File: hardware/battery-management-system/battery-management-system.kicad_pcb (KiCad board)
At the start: 4 copper layers, 100 x 111 mm, 212 parts, among them J1 CELL4_PLUS, J10 18V, J11 3V3, J12 AMPHENOL_micro_usb_10118194-0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, J13 I2C, J14 UART_INTERCONNECT, J15 LEDS, J16 CHARGE/DISCHARGE, J17 UART_USB, J18 rspro_header_5pin_3_5mm, J19 TEMP_CELL1, J2 CELL4_MINUS, J20 TEMP_CELL2, J21 TEMP_CELL3, J22 TEMP_CELL4, J23 Conn_01x05, J24 Charge, J25 Discharge, J3 CELL3_MINUS, J4 CELL2_MINUS, J5 CELL1_MINUS, J6 VBAT+, J7 VBAT+_CHARGE, J8 VBAT-, J9 5V, Q1 DMN3404L, Q10 DMN3404L, Q11 BS250FTA, Q12 BS250FTA, Q13 BS250FTA, Q14 BS250FTA, Q15 BS250FTA, Q16 DMN3404L, Q17 DMN3404L, Q18 DMN3404L, Q19 DMN3404L, Q2 TJ40S04M3L, Q20 DMN3404L, Q21 DMN3404L, Q22 DMN3404L, Q23 DMN3404L, Q24 DMN3404L, Q25 DMN3404L, Q26 DMN3404L, Q27 DMN3404L, Q28 DMN3404L, Q29 DMN3404L, Q3 TJ40S04M3L, Q30 DMN3404L, Q31 DMN3404L, Q32 DMN3404L, Q33 DMN3404L, Q34 DMN3404L, Q35 DMN3404L, Q36 DMN3404L, Q37 DMN3404L, Q38 DMN3404L, Q39 DMN3404L, Q4 DMN3404L, Q40 TJ40S04M3L, Q5 DMN3404L, Q6 DMN3404L, Q7 DMN3404L, Q8 DMN3404L, Q9 DMN3404L, U1 ICL7660, U10 STM32L071CZTx, U11 LM2904M8-13, U12 LM2904M8-13, U13 MC74VHC139, U2 L6982C33DR, U3 L6982C33DR, U4 ICL7660, U5 FT230XS, U6 ARM-JTAG-SWD, U7 AT24C512C, U8 NCT75DR2G, U9 STC3100

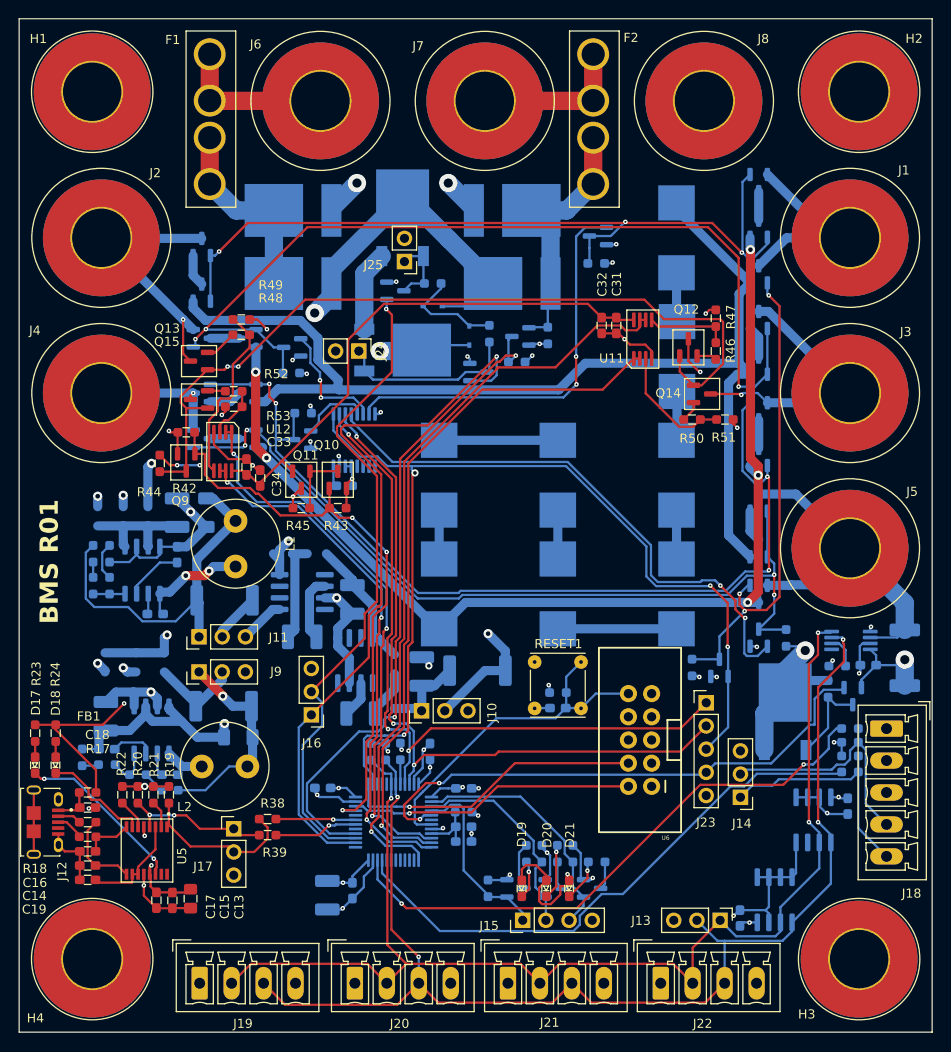
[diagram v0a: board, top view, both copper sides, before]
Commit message: update PCB from schematic
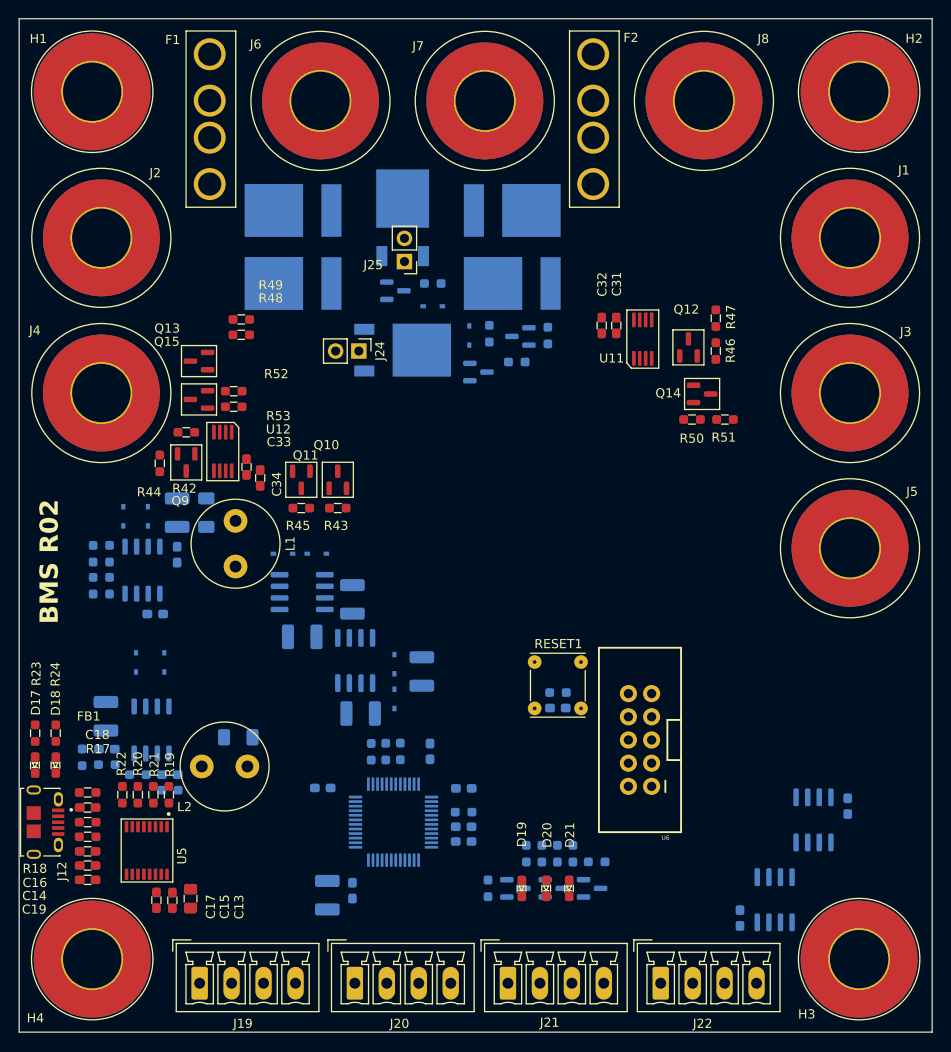
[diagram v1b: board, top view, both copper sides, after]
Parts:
- removed C30: 1uF, benediktibk:C_0603_1608Metric_Pad1.08x0.95mm_HandSolder
- removed C35: 100nF, benediktibk:C_0603_1608Metric_Pad1.08x0.95mm_HandSolder
- removed D15, D9: BAT54WS, benediktibk:D_SOD-323
- removed J10: 18V, benediktibk:PinHeader_1x03_P2.54mm_Vertical
- removed J11: 3V3, benediktibk:PinHeader_1x03_P2.54mm_Vertical
- removed J13: I2C, benediktibk:PinHeader_1x03_P2.54mm_Vertical
- removed J14: UART_INTERCONNECT, benediktibk:PinHeader_1x03_P2.54mm_Vertical
- removed J15: LEDS, benediktibk:PinHeader_1x04_P2.54mm_Vertical
- removed J16: CHARGE/DISCHARGE, benediktibk:PinHeader_1x03_P2.54mm_Vertical
- removed J17: UART_USB, benediktibk:PinHeader_1x03_P2.54mm_Vertical
- removed J18: rspro_header_5pin_3_5mm, benediktibk:rspro_header_5pin_3_5mm
- removed J23: Conn_01x05, benediktibk:PinHeader_1x05_P2.54mm_Vertical
- removed J9: 5V, benediktibk:PinHeader_1x03_P2.54mm_Vertical
- removed L10, L3, L4, L5, L6, L7, L8, L9: L_220µH_1A, benediktibk:L_Wuerth_HCI-1050
- removed Q16, Q17, Q18, Q19, Q20, Q21, Q22, Q23, Q24, Q25, Q26, Q27, Q28, Q29, Q30, Q31, Q32, Q33, Q34, Q35, Q36, Q37, Q38, Q39: DMN3404L, benediktibk:SOT-23
- removed Q40: TJ40S04M3L, benediktibk:TO-252-2
- removed R1, R14, R15, R16: 2mOhm, benediktibk:R_2512_6332Metric_Pad1.40x3.35mm_HandSolder
- removed R33: 200kOhm, benediktibk:R_0603_1608Metric_Pad0.98x0.95mm_HandSolder
- removed R35, R36, R38, R39: 0Ohm, benediktibk:R_0603_1608Metric_Pad0.98x0.95mm_HandSolder
- removed R40, R41, R54, R55, R56, R57, R58: 10kOhm, benediktibk:R_0603_1608Metric_Pad0.98x0.95mm_HandSolder
- removed R59: 220kOhm, benediktibk:R_0603_1608Metric_Pad0.98x0.95mm_HandSolder
- removed U13: MC74VHC139, benediktibk:TSSOP-16_4.4x5mm_P0.65mm
- removed U9: STC3100, benediktibk:MSOP-8_3x3mm_P0.65mm
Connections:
- C10 pad 1: Net-(D13-K) -> /18V
- C11 pad 1: Net-(J11-Pin_1) -> /3V3
- C12 pad 1: Net-(J9-Pin_1) -> Net-(D14-A)
- D13 pad 1: Net-(D13-K) -> /18V
- J5 pad 1: /Battery Pack/CELL1_MINUS -> GND
- L1 pad 1: Net-(J11-Pin_1) -> /3V3
- L2 pad 1: Net-(J9-Pin_1) -> Net-(D14-A)
- R10 pad 1: Net-(J9-Pin_1) -> Net-(D14-A)
- R6 pad 1: Net-(J11-Pin_1) -> /3V3
- U10 pad 21: Net-(U10-PB10) -> unconnected-(U10-PB10-Pad21)
- U10 pad 22: Net-(U10-PB11) -> unconnected-(U10-PB11-Pad22)
- U10 pad 30: Net-(U10-PA9) -> /MCU/UART_USB_TX
- U10 pad 31: Net-(U10-PA10) -> /MCU/UART_USB_RX
- U10 pad 38: /CELL_BALANCING_STROBE -> unconnected-(U10-PA15-Pad38)
- U10 pad 45: /CELL_BALANCING_A0 -> unconnected-(U10-PB8-Pad45)
- U10 pad 46: /CELL_BALANCING_A1 -> unconnected-(U10-PB9-Pad46)
- U10 pad 5: /EN_CELL_BALANCING -> unconnected-(U10-PH0-Pad5)
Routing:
- net GND: track 206.8 -> 0.00 mm, vias 41 -> 0
- net /18V: track 176.6 -> 0.00 mm, vias 8 -> 0
- net /5V_EXT: track 158.5 -> 0.00 mm, vias 2 -> 0
- net /MCU/SDA: track 136.1 -> 0.00 mm, vias 4 -> 0
- net /MCU/SCL: track 133.2 -> 0.00 mm, vias 3 -> 0
- net /5V: track 123.3 -> 0.00 mm, vias 3 -> 0
- net Net-(Q25-S): track 122.8 -> 0.00 mm
- net Net-(Q24-S): track 120.2 -> 0.00 mm, vias 5 -> 0
- net /CELL_BALANCING_STROBE: track 111.9 -> 0.00 mm, vias 4 -> 0
- net /PACK_EXT: track 104.5 -> 0.00 mm, vias 3 -> 0
- net /Cell Balancing/CHARGE_CELL2: track 103.4 -> 0.00 mm, vias 4 -> 0
- net /Cell Balancing/CHARGE_CELL3: track 101.9 -> 0.00 mm, vias 3 -> 0
- net /Battery Pack/PACK: track 95.8 -> 0.00 mm, vias 2 -> 0
- net /Cell Balancing/CHARGE_CELL1: track 91.8 -> 0.00 mm, vias 4 -> 0
- net Net-(Q12-G): track 91.1 -> 0.00 mm, vias 2 -> 0
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- removed copper zone on In1.Cu, net /3V3
- removed copper zone on In2.Cu, net GND
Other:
- board text added: "BMS R02"
- board text removed: "BMS R01"

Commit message: fix design errors
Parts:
- added C34: 100nF, benediktibk:C_0603_1608Metric_Pad1.08x0.95mm_HandSolder, F.Cu at (233.7, 96.5)
- added C35: 100nF, benediktibk:C_0603_1608Metric_Pad1.08x0.95mm_HandSolder, F.Cu at (233.7, 99.0)
- added C36: 100nF, benediktibk:C_0603_1608Metric_Pad1.08x0.95mm_HandSolder, F.Cu at (233.7, 101.5)
- added C37: 100nF, benediktibk:C_0603_1608Metric_Pad1.08x0.95mm_HandSolder, F.Cu at (233.7, 104.0)
- added R1: 220kOhm, benediktibk:R_0603_1608Metric_Pad0.98x0.95mm_HandSolder, F.Cu at (240.0, 96.5)
- added R3: 220kOhm, benediktibk:R_0603_1608Metric_Pad0.98x0.95mm_HandSolder, F.Cu at (240.0, 99.0)
- U2, U3: value L6982C33DR -> L6982CDR
- moved C2 108.6 mm to (145.9, 75.2)
- moved C31 108.6 mm to (192.4, 54.7)
- moved C5 108.6 mm to (145.9, 79.8)
- moved D1 108.6 mm to (177.9, 55.8)
- moved D14 108.6 mm to (141.4, 91.6)
- moved D17 108.6 mm to (183.6, 116.3)
- moved D2 108.6 mm to (173.9, 52.6)
- moved FB2 108.6 mm to (177.2, 108.0)
- moved Q1 108.6 mm to (178.9, 59.8)
- moved Q12 108.6 mm to (201.9, 57.1)
- moved Q14 108.6 mm to (203.4, 62.2)
- moved Q7 108.6 mm to (187.1, 116.3)
- moved Q9 108.6 mm to (146.9, 69.7)
- moved R20 108.6 mm to (139.9, 106.1)
- moved R24 108.6 mm to (184.1, 112.5)
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- renumbered C31 to C30, C32 to C31, C33 to C32, C34 to C33, D11 to D10, D12 to D11, D13 to D12, D14 to D13, D16 to D14, D17 to D15, D18 to D16, D19 to D17, D20 to D18, D21 to D19, D10 to D9, J8 to J10, J12 to J11, J19 to J12, J20 to J13, J21 to J14, J22 to J15, J24 to J6, J25 to J7, J6 to J8, J7 to J9, R9 to R10, R10 to R11, R11 to R12, R12 to R13, R13 to R14, R17 to R15, R18 to R16, R19 to R17, R20 to R18, R21 to R19, R22 to R20, R23 to R21, R24 to R22, R25 to R23, R26 to R24, R27 to R25, R28 to R26, R29 to R27, R30 to R28, R31 to R29, R32 to R30, R34 to R31, R37 to R32, R42 to R33, R43 to R34, R44 to R35, R45 to R36, R46 to R37, R47 to R38, R48 to R39, R3 to R4, R49 to R40, R50 to R41, R51 to R42, R52 to R43, R53 to R44, R4 to R5, R5 to R6, R6 to R7, R7 to R8, R8 to R9, U11 to U10, U12 to U11, U10 to U9
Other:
- board size 100 x 111 mm -> 100 x 100 mm

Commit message: fix design errors
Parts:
- removed the D5 at (158.6, 42.1)
- removed the D6 at (182.6, 42.1)
- removed the J10 at (203.6, 30.1)
- removed the J2 at (137.6, 45.1)
- removed the J3 at (219.6, 62.1)
- removed the J8 at (161.6, 30.1)
- removed the J9 at (179.6, 30.1)
- J1: value CELL4_PLUS -> CELLS; footprint benediktibk:Connector_M6 -> benediktibk:rspro_header_5pin_5_08mm
- J4: value CELL2_MINUS -> VBAT_DISCHARGE; footprint benediktibk:Connector_M6 -> benediktibk:rspro_header_2pin_5_08mm
- J5: value CELL1_MINUS -> VBAT_CHARGE; footprint benediktibk:Connector_M6 -> benediktibk:rspro_header_2pin_5_08mm
- J7: renamed from U6; footprint benediktibk:ARM-JTAG-10-SWD-IDC -> benediktibk:SAMTEC_FTSH-105-01-F-DV-P-TR
- moved J1 170.5 mm to (50.0, 27.0)
- moved J5 133.2 mm to (97.0, 27.0)
- moved J8 109.2 mm to (39.8, 114.6)
- moved D13 104.9 mm to (26.1, 90.8)
- moved D14 104.9 mm to (28.4, 90.8)
- moved J6 104.9 mm to (26.0, 97.0)
- moved R21 104.9 mm to (26.1, 87.2)
- moved R22 104.9 mm to (28.4, 87.2)
- moved R20 102.8 mm to (37.8, 93.4)
- moved C13 102.8 mm to (45.3, 104.8)
- moved C14 102.8 mm to (34.0, 101.2)
- moved C15 102.8 mm to (43.3, 105.0)
- moved C16 102.8 mm to (34.0, 99.6)
- moved C17 102.8 mm to (41.5, 105.0)
- moved C18 102.8 mm to (34.0, 94.8)
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- renumbered D12 to D10, D13 to D11, D14 to D12, D15 to D13, D16 to D14, D17 to D15, D18 to D16, D19 to D17, D7 to D5, D8 to D6, D9 to D7, D10 to D8, D11 to D9, J14 to J10, J15 to J11, J6 to J2, J7 to J3, J11 to J6, J12 to J8, J13 to J9, U11 to U10, U7 to U6, U8 to U7, U9 to U8, U10 to U9
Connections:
- F1 pad 1: Net-(J8-Pin_1) -> Net-(J4-Pin_1)
- F2 pad 1: Net-(J9-Pin_1) -> Net-(J5-Pin_1)
- J4 pad 1: /Battery Pack/CELL2_MINUS -> Net-(J4-Pin_1)
- J5 pad 1: GND -> Net-(J5-Pin_1)

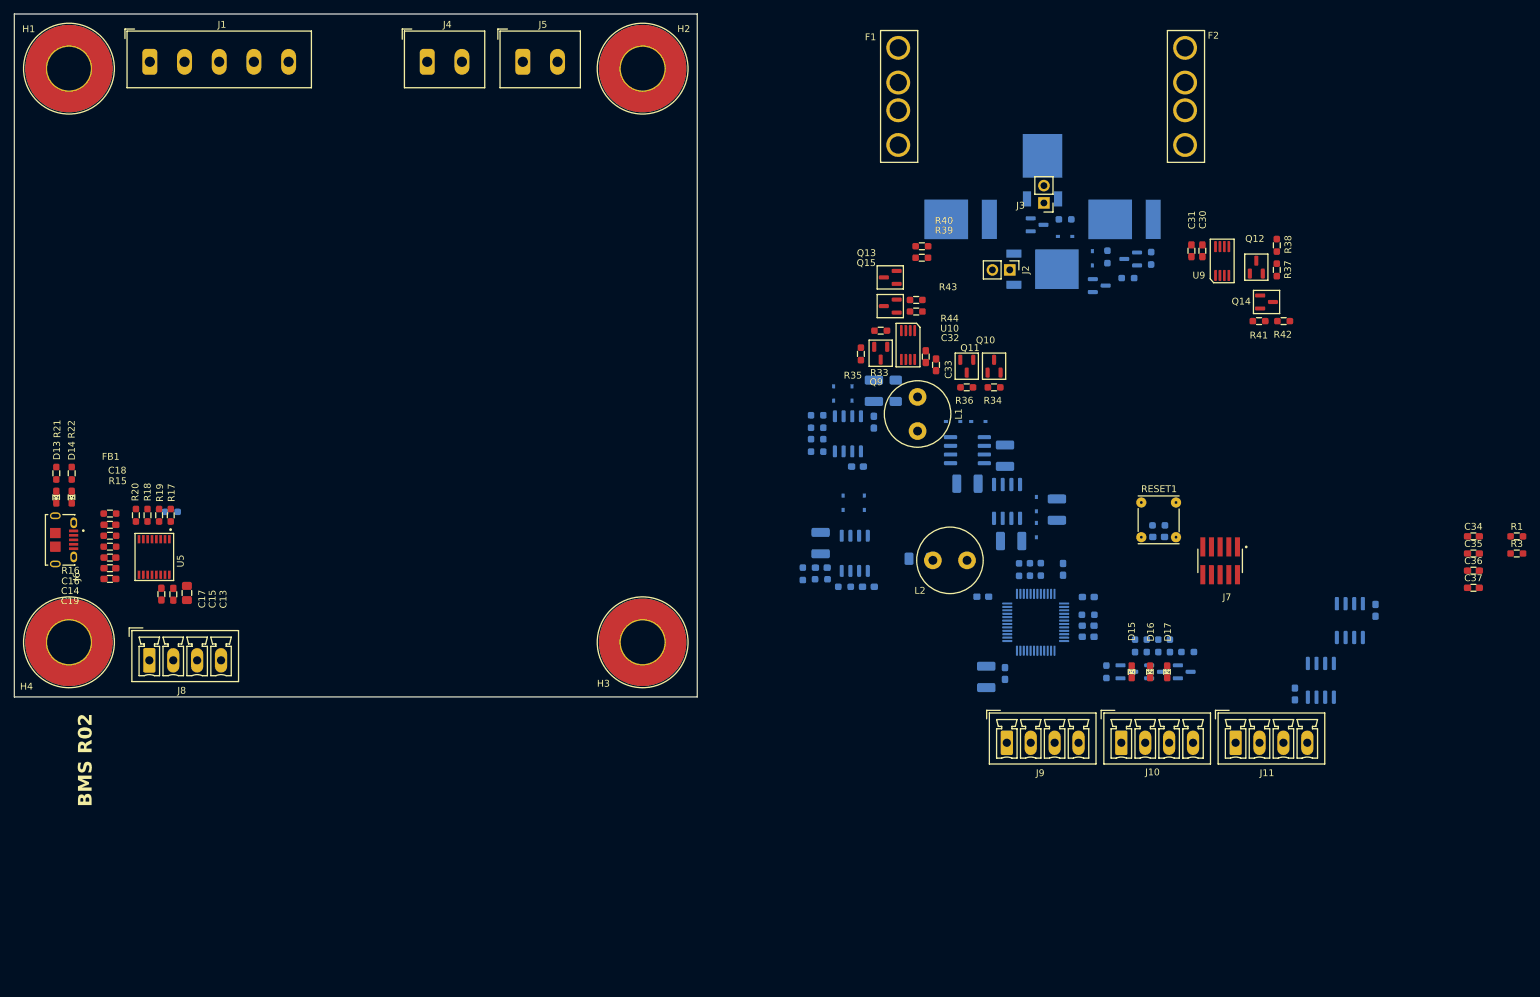
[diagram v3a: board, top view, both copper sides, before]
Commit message: add heatsink and fix ERC errors
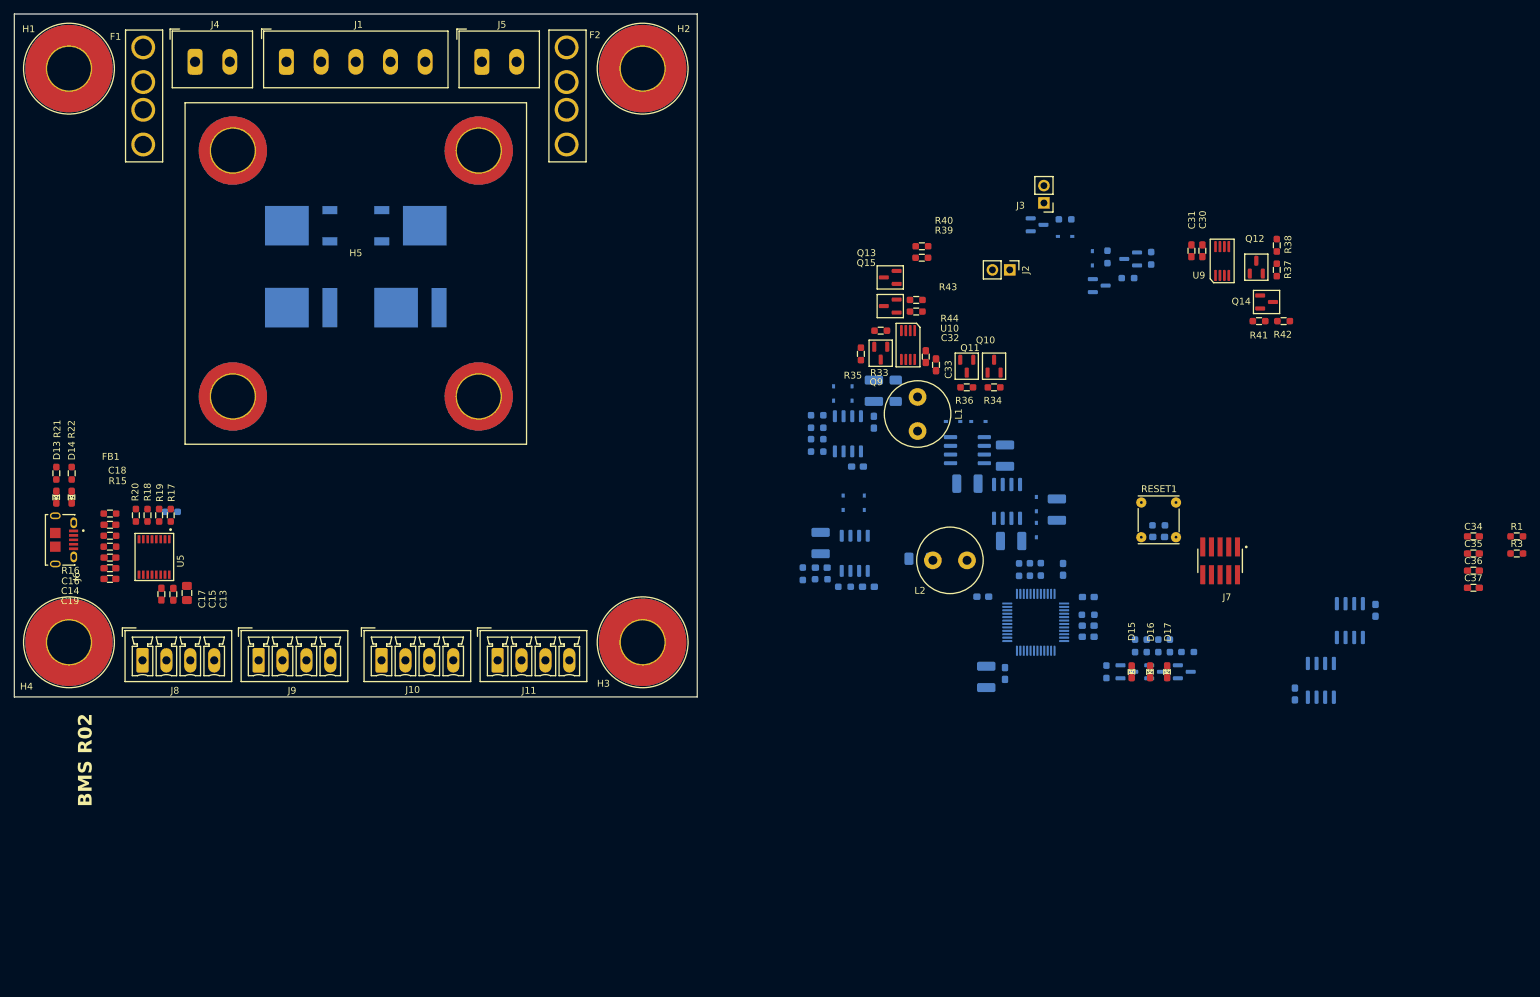
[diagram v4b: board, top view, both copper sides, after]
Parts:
- added H5: heatsink_50x50, benediktibk:heatsink_50x50, F.Cu at (70.0, 58.0)
- moved F1 110.6 mm to (37.3, 32.0)
- moved J9 110.2 mm to (55.8, 114.6)
- moved J10 109.0 mm to (73.8, 114.6)
- moved Q2 108.7 mm to (62.0, 51.0), turned to 180 degrees
- moved J11 108.7 mm to (90.8, 114.6)
- moved D4 105.4 mm to (78.0, 63.0)
- moved D3 97.4 mm to (62.0, 63.0)
- moved Q3 92.9 mm to (78.0, 51.0), turned to 0 degrees
- moved F2 90.6 mm to (99.3, 32.0)
- moved J4 34.0 mm to (49.0, 27.0)
- moved J1 20.0 mm to (70.0, 27.0)
- moved J5 6.00 mm to (91.0, 27.0)
- moved J8 1.00 mm to (38.8, 114.6)
